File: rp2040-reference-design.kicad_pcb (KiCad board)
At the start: 4 copper layers, 29.5 x 27 mm, 36 parts, among them J2 Conn_01x10_Pin, J3 Conn_01x10_Pin, U1 RP2040, U2 W25Q128JVS, Y1 12mhz ABM8-272-T

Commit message: fix: drc
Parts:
- renumbered BMDU to J1, Reset to SW1, Boot to SW2
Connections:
- R6 pad 1: unconnected-(R6-Pad1) -> Net-(R6-Pad1)
- SW2 pad 2: unconnected-(SW2-Pad2) -> Net-(R6-Pad1)
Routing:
- net Net-(R6-Pad1): track 0.00 -> 25.3 mm, vias 0 -> 2
- net (no net): track 25.3 -> 0.00 mm, vias 2 -> 0

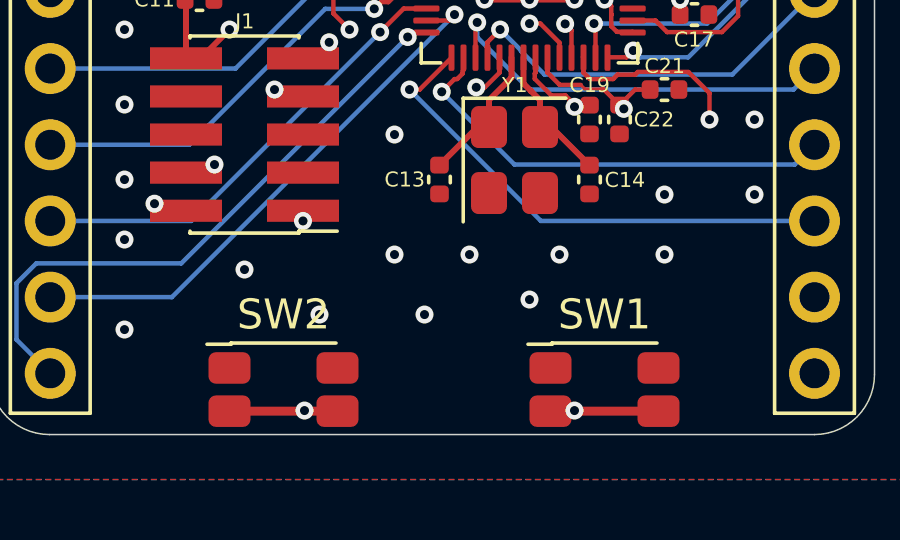
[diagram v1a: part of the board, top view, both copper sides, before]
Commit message: fix: button text
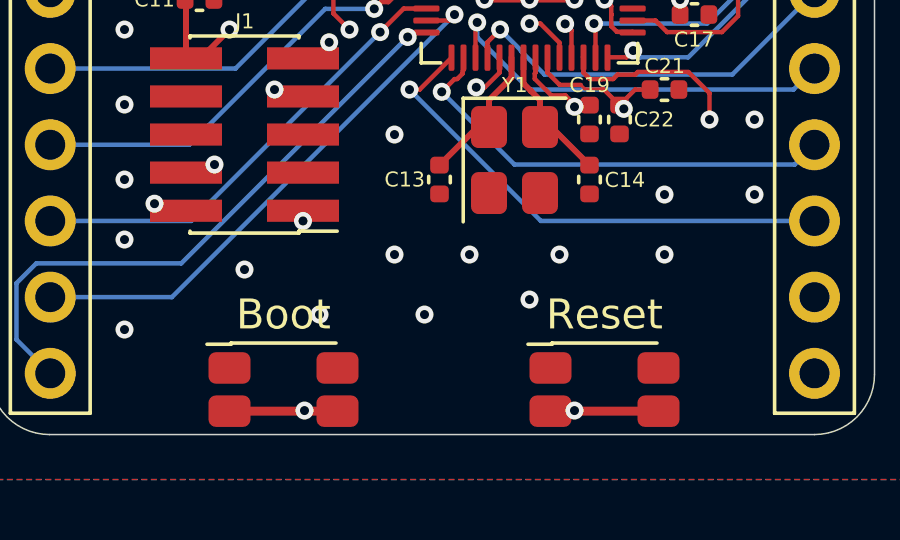
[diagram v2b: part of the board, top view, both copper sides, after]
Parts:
- renumbered SW2 to Boot, SW1 to Reset
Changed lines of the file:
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@@
 	(net 52 "GPIO23")
 	(net 53 "unconnected-(U1-USB_DP-Pad47)")
-	(net 54 "Net-(R6-Pad1)")
+	(net 54 "Net-(Boot1-Pad2)")
 	(footprint "Capacitor_SMD:C_0402_1005Metric"
 		(layer "F.Cu")
@@
 		(descr "Light Touch Switch, 2.2 N, https://www3.panasonic.biz/ac/e_download/control/switch/light-touch/catalog/sw_lt_eng_3529s_side.pdf?f_cd=402906")
 		(tags "tactile switch")
-		(property "Reference" "SW1"
+		(property "Reference" "Reset"
 			(at 0 -2.5 0)
 			(layer "F.SilkS")
@@
 		(descr "Light Touch Switch, 2.2 N, https://www3.panasonic.biz/ac/e_download/control/switch/light-touch/catalog/sw_lt_eng_3529s_side.pdf?f_cd=402906")
 		(tags "tactile switch")
-		(property "Reference" "SW2"
+		(property "Reference" "Boot"
 			(at 0 -2.5 0)
 			(layer "F.SilkS")
@@
 			(layers "F.Cu" "F.Mask" "F.Paste")
 			(roundrect_rratio 0.2380952381)
-			(net 54 "Net-(R6-Pad1)")
+			(net 54 "Net-(Boot1-Pad2)")
 			(pinfunction "2")
 			(pintype "passive")
@@
 			(layers "F.Cu" "F.Mask" "F.Paste")
 			(roundrect_rratio 0.2380952381)
-			(net 54 "Net-(R6-Pad1)")
+			(net 54 "Net-(Boot1-Pad2)")
 			(pinfunction "2")
 			(pintype "passive")
@@
 			(layers "F.Cu" "F.Mask" "F.Paste")
 			(roundrect_rratio 0.25)
-			(net 54 "Net-(R6-Pad1)")
+			(net 54 "Net-(Boot1-Pad2)")
 			(pintype "passive")
 		)

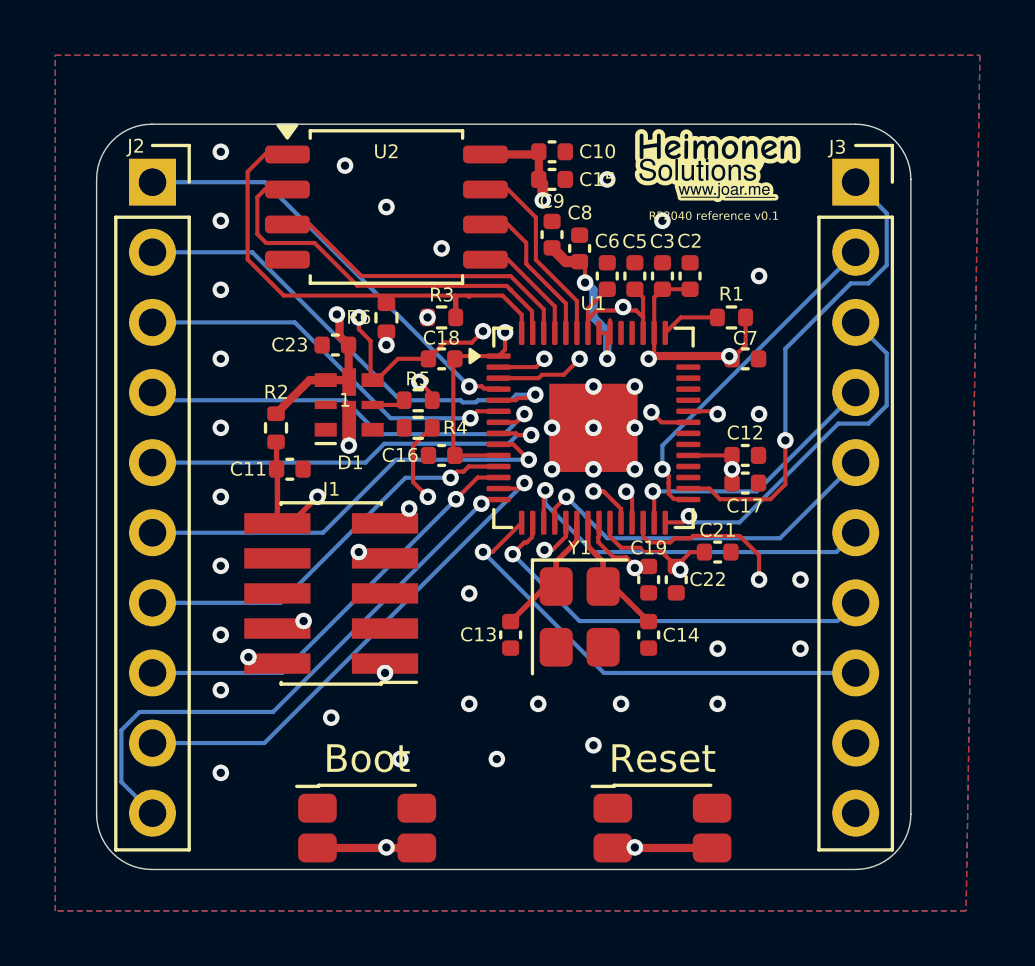
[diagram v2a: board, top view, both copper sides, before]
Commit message: feat: added pin numbers
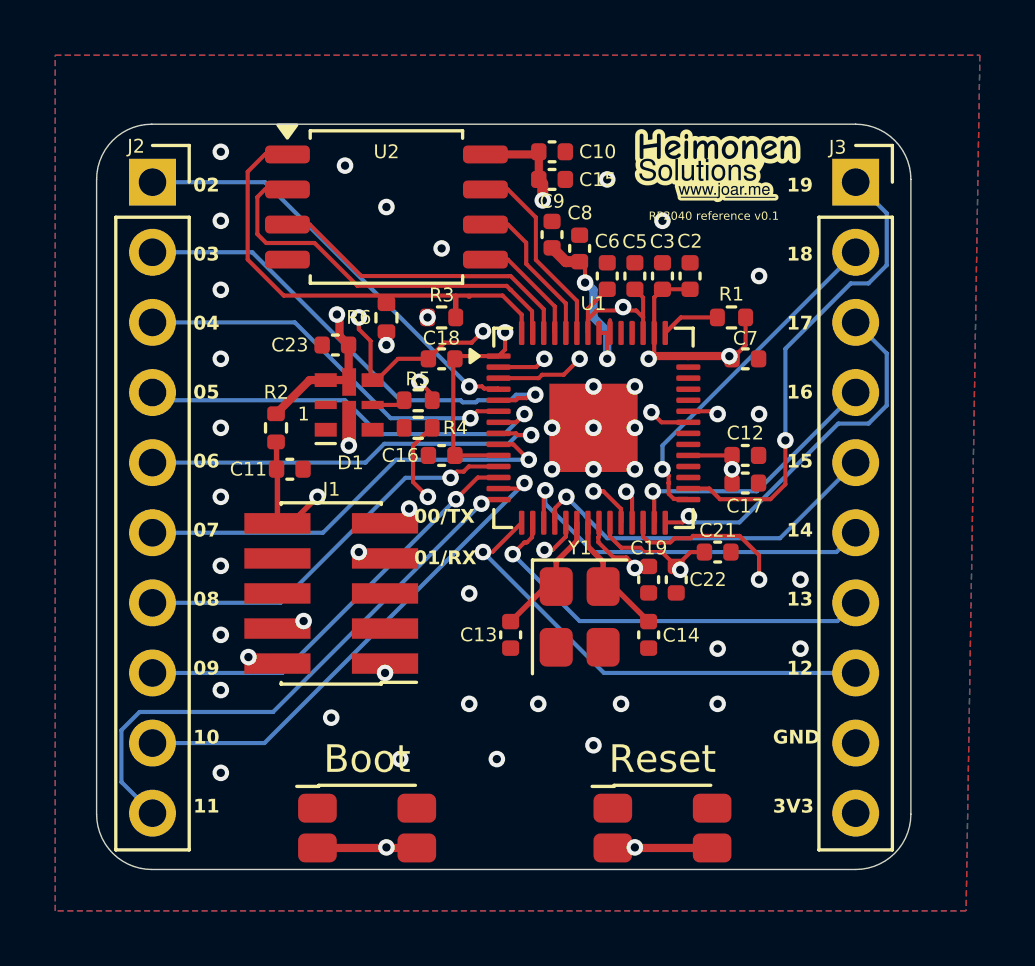
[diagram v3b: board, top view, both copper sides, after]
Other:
- board text added: "00/TX"
- board text added: "01/RX"
- board text added: "02"
- board text added: "03"
- board text added: "04"
- board text added: "05"
- board text added: "06"
- board text added: "07"
- board text added: "08"
- board text added: "09"
- board text added: "10"
- board text added: "11"
- board text added: "12"
- board text added: "13"
- board text added: "14"
- board text added: "15"
- board text added: "16"
- board text added: "17"
- board text added: "18"
- board text added: "19"
- board text added: "3V3"
- board text added: "GND"

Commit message: feat: removed traces from underside of clock
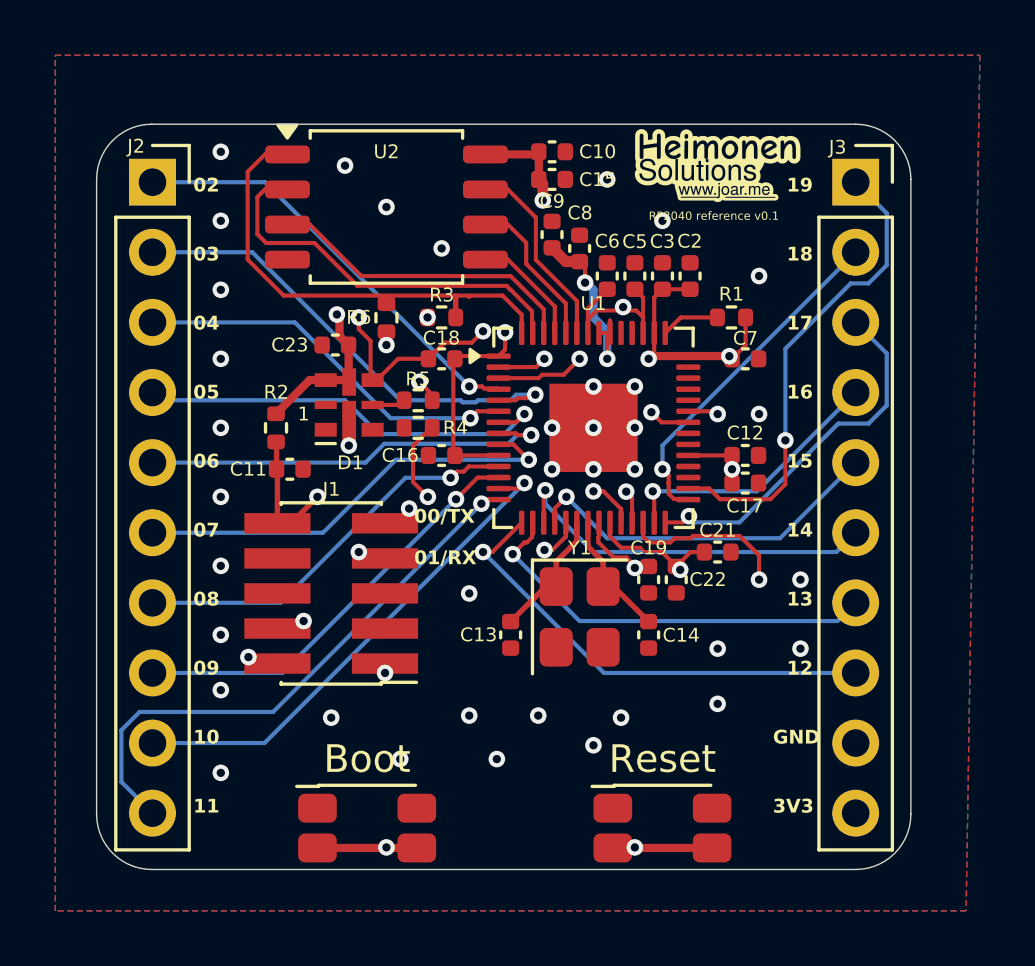
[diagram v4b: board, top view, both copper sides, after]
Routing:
- net IOVDD: track 88.9 -> 92.1 mm
- net nRst: track 47.2 -> 46.6 mm
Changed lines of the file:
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@@
 	)
 	(via
-		(at 124.5 106.5)
+		(at 124.5 106.925)
 		(size 0.6)
 		(drill 0.3)
@@
 	)
 	(via
-		(at 122 106.5)
+		(at 122 106.925)
 		(size 0.6)
 		(drill 0.3)
@@
 	)
 	(via
-		(at 127.5 106.5)
+		(at 127.5 107)
 		(size 0.6)
 		(drill 0.3)
@@
 	)
 	(segment
+		(start 128 101.575)
+		(end 128.5 102.075)
+		(width 0.15)
+		(layer "In1.Cu")
+		(net 2)
+	)
+	(segment
+		(start 126.354611 105.649)
+		(end 126.003611 106)
+		(width 0.15)
+		(layer "In1.Cu")
+		(net 2)
+	)
+	(segment
 		(start 120.641 92.349)
 		(end 120.49 92.5)
@@
 	)
 	(segment
+		(start 126.003611 106)
+		(end 119.57 106)
+		(width 0.15)
+		(layer "In1.Cu")
+		(net 2)
+	)
+	(segment
 		(start 126.197335 91.240878)
 		(end 126.197335 91.197335)
@@
 	)
 	(segment
+		(start 128.5 102.075)
+		(end 128.5 105.003612)
+		(width 0.15)
+		(layer "In1.Cu")
+		(net 2)
+	)
+	(segment
 		(start 131.746525 97.773475)
 		(end 131.746525 94.226525)
@@
 	)
 	(segment
-		(start 119.33 105)
-		(end 118.95 105.38)
-		(width 0.15)
-		(layer "In1.Cu")
-		(net 2)
-	)
-	(segment
 		(start 131.52 99.717019)
 		(end 131.52 98)
@@
 	)
 	(segment
-		(start 124.575 105)
-		(end 119.33 105)
-		(width 0.15)
-		(layer "In1.Cu")
-		(net 2)
-	)
-	(segment
 		(start 131.746525 94.226525)
 		(end 131.576 94.056)
@@
 	)
 	(segment
+		(start 128.5 105.003612)
+		(end 127.854612 105.649)
+		(width 0.15)
+		(layer "In1.Cu")
+		(net 2)
+	)
+	(segment
 		(start 126.197335 91.197335)
 		(end 125 90)
@@
 	)
 	(segment
-		(start 128 101.575)
-		(end 124.575 105)
+		(start 127.854612 105.649)
+		(end 126.354611 105.649)
 		(width 0.15)
 		(layer "In1.Cu")
@@
 		(end 120.641 92.349)
 		(width 0.3)
+		(layer "In1.Cu")
+		(net 2)
+	)
+	(segment
+		(start 119.57 106)
+		(end 118.95 105.38)
+		(width 0.15)
 		(layer "In1.Cu")
 		(net 2)
@@
 	)
 	(segment
+		(start 117 99.5)
+		(end 117 105)
+		(width 0.15)
+		(layer "In1.Cu")
+		(net 4)
+	)
+	(segment
+		(start 125 107.5)
+		(end 126.5 106)
+		(width 0.15)
+		(layer "In1.Cu")
+		(net 4)
+	)
+	(segment
+		(start 128 106)
+		(end 128.305878 105.694122)
+		(width 0.15)
+		(layer "In1.Cu")
+		(net 4)
+	)
+	(segment
+		(start 129 103.5)
+		(end 129 105)
+		(width 0.15)
+		(layer "In1.Cu")
+		(net 4)
+	)
+	(segment
+		(start 117 105)
+		(end 119.5 107.5)
+		(width 0.15)
+		(layer "In1.Cu")
+		(net 4)
+	)
+	(segment
+		(start 116.5 99)
+		(end 117 99.5)
+		(width 0.15)
+		(layer "In1.Cu")
+		(net 4)
+	)
+	(segment
+		(start 128.305878 105.694122)
+		(end 128.305878 111.394122)
+		(width 0.15)
+		(layer "In1.Cu")
+		(net 4)
+	)
+	(segment
+		(start 126.5 106)
+		(end 128 106)
+		(width 0.15)
+		(layer "In1.Cu")
+		(net 4)
+	)
+	(segment
 		(start 130.5 102)
-		(end 128.305878 104.194122)
-		(width 0.15)
-		(layer "In1.Cu")
-		(net 4)
-	)
-	(segment
-		(start 125 107.5)
-		(end 128.305878 104.194122)
+		(end 129 103.5)
+		(width 0.15)
+		(layer "In1.Cu")
+		(net 4)
+	)
+	(segment
+		(start 132.5 102)
+		(end 130.5 102)
+		(width 0.15)
+		(layer "In1.Cu")
+		(net 4)
+	)
+	(segment
+		(start 128.305878 111.394122)
+		(end 128 111.7)
 		(width 0.15)
 		(layer "In1.Cu")
@@
 	)
 	(segment
-		(start 116.5 99)
-		(end 117 99.5)
-		(width 0.15)
-		(layer "In1.Cu")
-		(net 4)
-	)
-	(segment
-		(start 132.5 102)
-		(end 130.5 102)
-		(width 0.15)
-		(layer "In1.Cu")
-		(net 4)
-	)
-	(segment
-		(start 128.305878 104.194122)
-		(end 128.305878 111.394122)
-		(width 0.15)
-		(layer "In1.Cu")
-		(net 4)
-	)
-	(segment
-		(start 117 99.5)
-		(end 117 105)
-		(width 0.15)
-		(layer "In1.Cu")
-		(net 4)
-	)
-	(segment
-		(start 128.305878 111.394122)
-		(end 128 111.7)
-		(width 0.15)
-		(layer "In1.Cu")
-		(net 4)
-	)
-	(segment
-		(start 117 105)
-		(end 119.5 107.5)
-		(width 0.15)
-		(layer "In1.Cu")
+		(start 129 105)
+		(end 128.305878 105.694122)
+		(width 0.15)
+		(layer "In1.Cu")

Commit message: fix: removed unused via
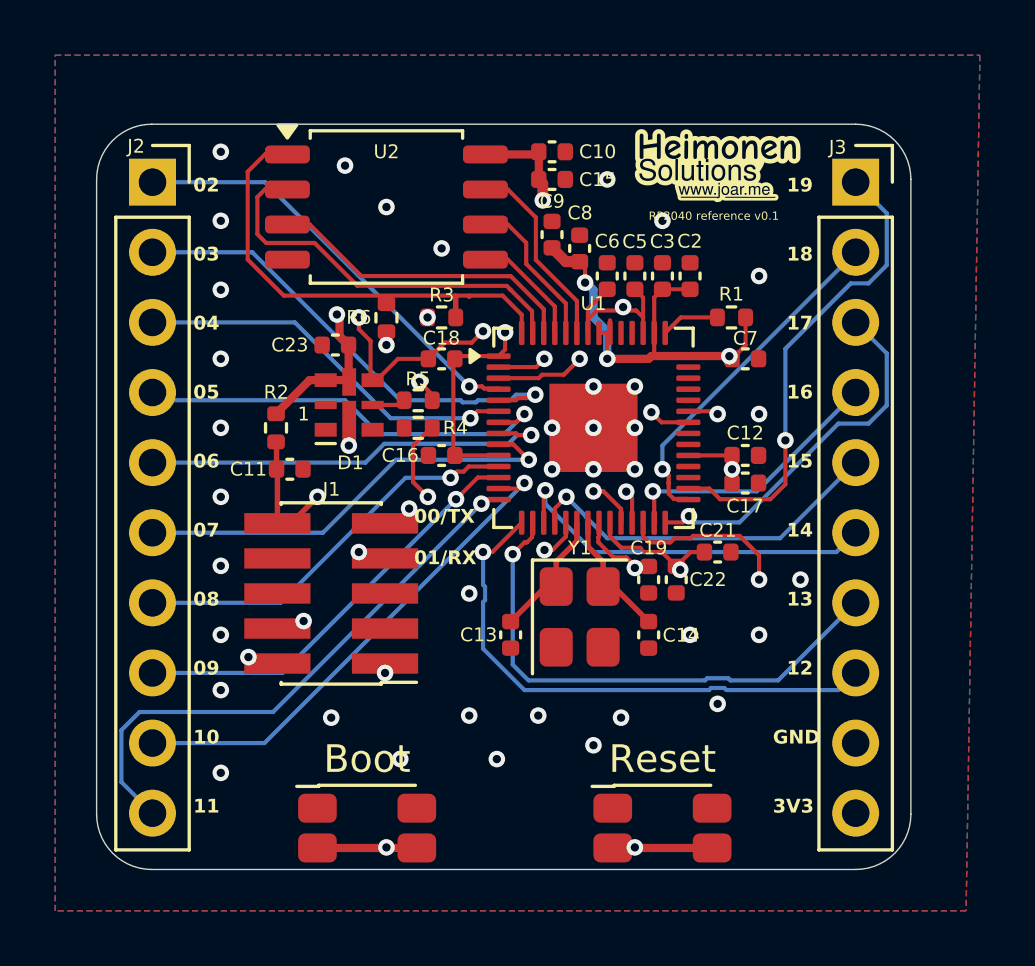
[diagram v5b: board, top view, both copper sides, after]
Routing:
- net GPIO13: track 15.2 -> 19.4 mm
- net GPIO12: track 17.2 -> 19.8 mm
- net IOVDD: track 92.1 -> 91.9 mm, vias 11 -> 10
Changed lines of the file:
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@@
 	)
 	(via
-		(at 134 104.5)
+		(at 132.5 104)
 		(size 0.6)
 		(drill 0.3)
@@
 	)
 	(via
-		(at 131 104.5)
+		(at 130 104)
 		(size 0.6)
 		(drill 0.3)
@@
 	)
 	(segment
+		(start 128.6 93.9)
+		(end 128.5 94)
+		(width 0.3)
+		(layer "F.Cu")
+		(net 2)
+	)
+	(segment
 		(start 126.197335 90.677335)
 		(end 126 90.48)
@@
 	)
 	(segment
-		(start 128.5 94)
-		(end 128.7 93.8)
-		(width 0.15)
-		(layer "F.Cu")
-		(net 2)
-	)
-	(segment
 		(start 117.301 92.487827)
 		(end 117.301 93.171)
@@
 		(end 126.7 100.43742)
 		(width 0.15)
+		(layer "F.Cu")
+		(net 2)
+	)
+	(segment
+		(start 128.5 94)
+		(end 127 94)
+		(width 0.3)
 		(layer "F.Cu")
 		(net 2)
@@
 	)
 	(segment
-		(start 128.5 94)
-		(end 128.6 93.9)
-		(width 0.15)
-		(layer "F.Cu")
-		(net 2)
-	)
-	(segment
 		(start 132.01 93.51)
 		(end 131.52 94)
@@
 	)
 	(via
-		(at 128.5 94)
-		(size 0.6)
-		(drill 0.3)
-		(layers "F.Cu" "B.Cu")
-		(net 2)
-	)
-	(via
 		(at 131.52 98)
 		(size 0.6)
@@
 		(start 117.730346 91.849)
 		(end 117.207068 92.372278)
-		(width 0.3)
-		(layer "In1.Cu")
-		(net 2)
-	)
-	(segment
-		(start 127 94)
-		(end 128.5 94)
 		(width 0.3)
 		(layer "In1.Cu")
@@
 	)
 	(segment
-		(start 126.88 105.38)
+		(start 122.576 102.261412)
+		(end 122.5 102.185412)
+		(width 0.15)
+		(layer "B.Cu")
+		(net 28)
+	)
+	(segment
+		(start 122.576 102.738588)
+		(end 122.576 102.261412)
+		(width 0.15)
+		(layer "B.Cu")
+		(net 28)
+	)
+	(segment
+		(start 131.314588 106)
+		(end 131.238588 105.924)
+		(width 0.15)
+		(layer "B.Cu")
+		(net 28)
+	)
+	(segment
+		(start 124 106)
+		(end 122.5 104.5)
+		(width 0.15)
+		(layer "B.Cu")
+		(net 28)
+	)
+	(segment
+		(start 130.685412 106)
+		(end 124 106)
+		(width 0.15)
+		(layer "B.Cu")
+		(net 28)
+	)
+	(segment
+		(start 122.5 102.185412)
 		(end 122.5 101)
 		(width 0.15)
@@
 	)
 	(segment
+		(start 131.238588 105.924)
+		(end 130.761412 105.924)
+		(width 0.15)
+		(layer "B.Cu")
+		(net 28)
+	)
+	(segment
 		(start 136 105.38)
-		(end 126.88 105.38)
+		(end 135.38 106)
+		(width 0.15)
+		(layer "B.Cu")
+		(net 28)
+	)
+	(segment
+		(start 130.761412 105.924)
+		(end 130.685412 106)
+		(width 0.15)
+		(layer "B.Cu")
+		(net 28)
+	)
+	(segment
+		(start 135.38 106)
+		(end 131.314588 106)
+		(width 0.15)
+		(layer "B.Cu")
+		(net 28)
+	)
+	(segment
+		(start 122.5 102.814588)
+		(end 122.576 102.738588)
+		(width 0.15)
+		(layer "B.Cu")
+		(net 28)
+	)
+	(segment
+		(start 122.5 104.5)
+		(end 122.5 102.814588)
 		(width 0.15)
 		(layer "B.Cu")
@@
 	)
 	(segment
-		(start 126 103.5)
-		(end 135.34 103.5)
+		(start 130.540023 105.649)
+		(end 130.616024 105.573)
 		(width 0.15)
 		(layer "B.Cu")
@@
 	)
 	(segment
+		(start 131.459977 105.649)
+		(end 133.191 105.649)
+		(width 0.15)
+		(layer "B.Cu")
+		(net 29)
+	)
+	(segment
+		(start 130.616024 105.573)
+		(end 131.383976 105.573)
+		(width 0.15)
+		(layer "B.Cu")
+		(net 29)
+	)
+	(segment
+		(start 131.383976 105.573)
+		(end 131.459977 105.649)
+		(width 0.15)
+		(layer "B.Cu")
+		(net 29)
+	)
+	(segment
+		(start 133.191 105.649)
+		(end 136 102.84)
+		(width 0.15)
+		(layer "B.Cu")
+		(net 29)
+	)
+	(segment
+		(start 124.145388 105.649)
+		(end 130.540023 105.649)
+		(width 0.15)
+		(layer "B.Cu")
+		(net 29)
+	)
+	(segment
 		(start 123.575337 101.075337)
-		(end 126 103.5)
+		(end 123.575337 105.078949)
 		(width 0.15)
 		(layer "B.Cu")
@@
 	)
 	(segment
-		(start 135.34 103.5)
-		(end 136 102.84)
-		(width 0.15)
-		(layer "B.Cu")
+		(start 123.575337 105.078949)
+		(end 124.145388 105.649)
+		(width 0.15)
+		(layer "B.Cu")

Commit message: feat: small improvements
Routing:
- net nRst: track 46.6 -> 43.2 mm, vias 3 -> 0
- net GPIO19: track 17.2 -> 15.9 mm, vias 1 -> 0
- net Net-(Boot1-Pad2): track 25.3 -> 24.6 mm
- net GND: vias 41 -> 37
